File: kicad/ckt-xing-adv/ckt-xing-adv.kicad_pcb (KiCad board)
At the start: 2 copper layers, 76.2 x 63.5 mm, 49 parts, among them J1 Screw_Terminal_01x02, J2 SM04B-SRSS, J3 Conn_02x05_Counter_Clockwise, J4 SM04B-SRSS, J5 SM04B-SRSS, J6 Screw_Terminal_01x02, J7 Screw_Terminal_01x02, Q1 ZXMS6004FF, Q2 ZXMS6004FF, SW1 SW_DIP_x05, U1 PAM8301, U2 ATtiny861A-S, U3 AP7381-33Y, U4 W25Q128JVS

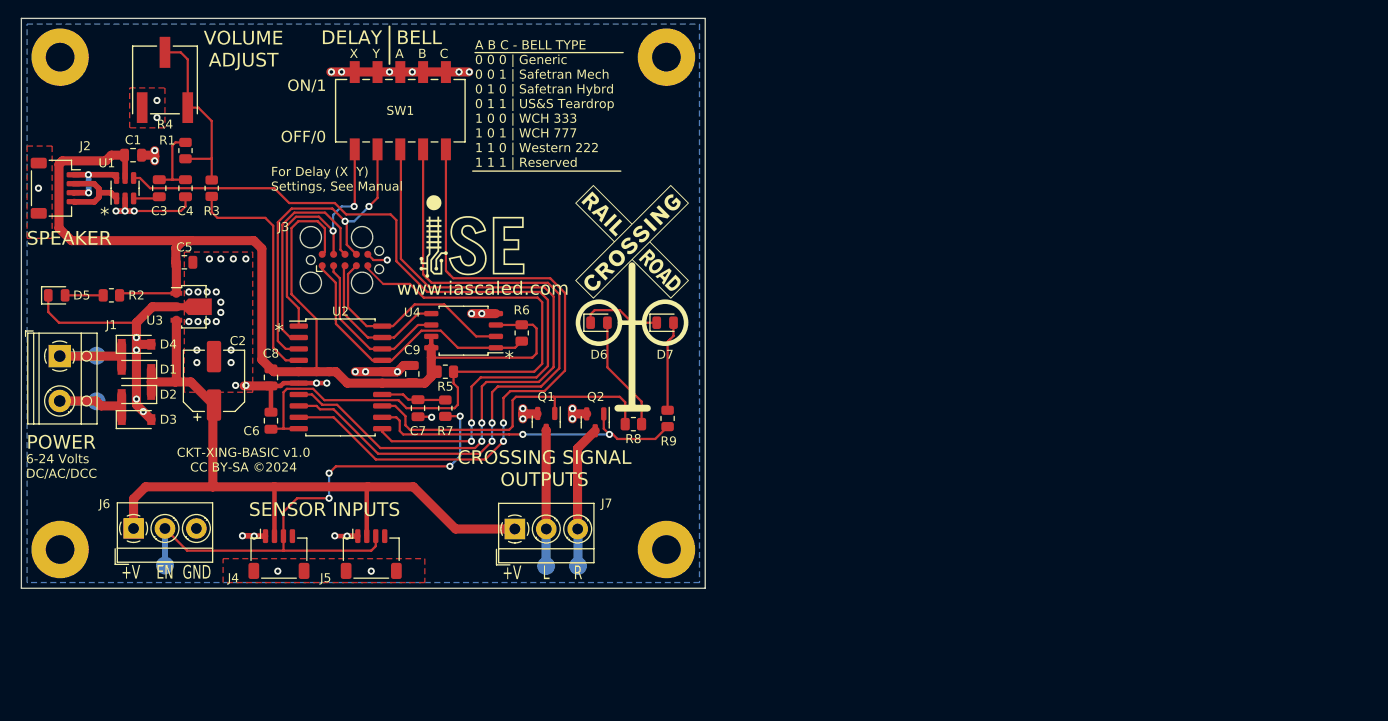
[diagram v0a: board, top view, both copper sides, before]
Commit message: Update advanced crossing with some fixes before PCB layout
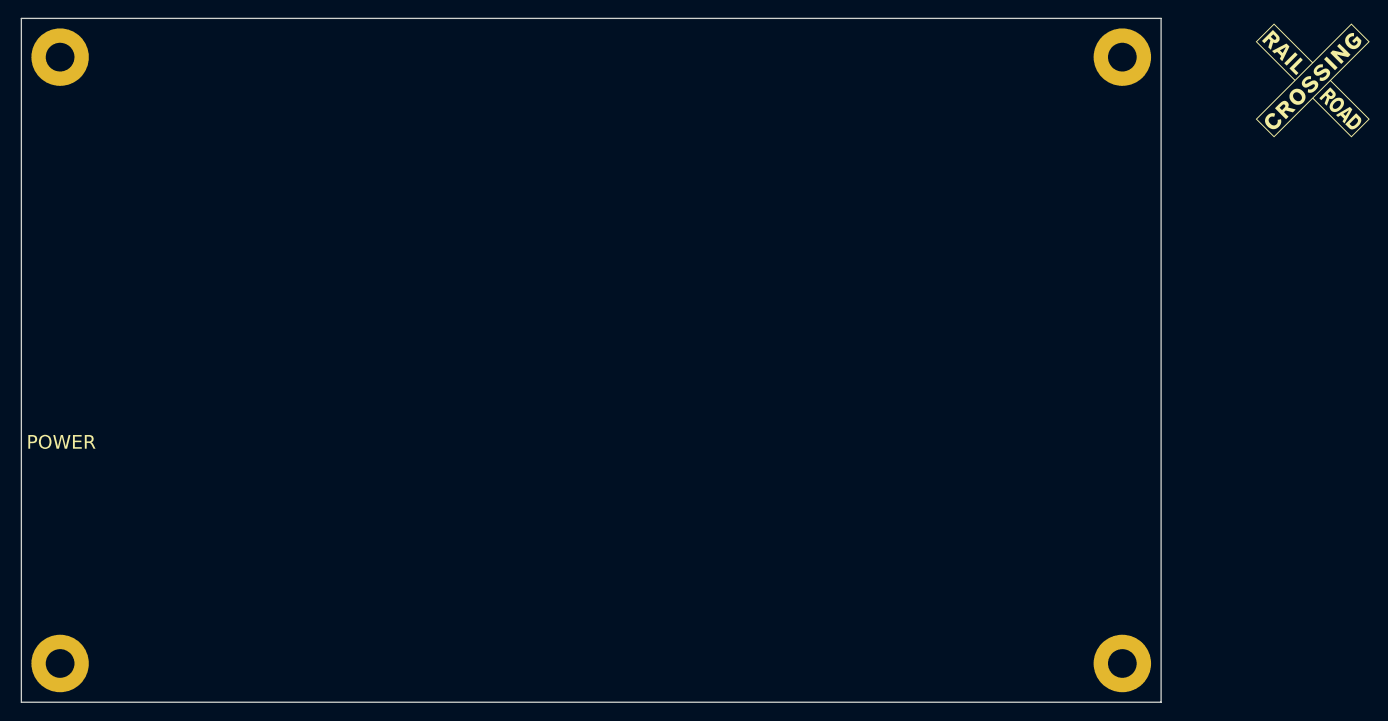
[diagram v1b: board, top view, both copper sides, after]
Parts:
- removed C1: 10uF, Capacitor_SMD:C_0805_2012Metric
- removed C2: 68uF, Capacitor_SMD:CP_Elec_6.3x5.8
- removed C3, C8, C9: 0.1uF, Capacitor_SMD:C_0805_2012Metric
- removed C4: 470pF, Capacitor_SMD:C_0805_2012Metric
- removed C5: 22uF, Capacitor_SMD:C_0805_2012Metric
- removed C6, C7: 1uF, Capacitor_SMD:C_0805_2012Metric
- removed D1, D2, D3, D4: CDBM140G, Diode_SMD:D_SOD-123
- removed D5: GREEN LED, LED_SMD:LED_0805_2012Metric
- removed D6, D7: RED LED, LED_SMD:LED_0805_2012Metric
- removed J1: Screw_Terminal_01x02, TerminalBlock_RND:TerminalBlock_RND_205-00012_1x02_P5.00mm_Horizontal
- removed J2, J4, J5: SM04B-SRSS, Connector_JST:JST_SH_SM04B-SRSS-TB_1x04-1MP_P1.00mm_Horizontal
- removed J3: Conn_02x05_Counter_Clockwise, Connector:Tag-Connect_TC2050-IDC-FP_2x05_P1.27mm_Vertical
- removed J6, J7: Screw_Terminal_01x02, TerminalBlock_MetzConnect:TerminalBlock_MetzConnect_Type059_RT06303HBWC_1x03_P3.50mm_Horizontal
- removed Q1, Q2: ZXMS6004FF, Package_TO_SOT_SMD:SOT-23
- removed R1: 100k, Resistor_SMD:R_0805_2012Metric
- removed R2, R7, R8, R9: 1k, Resistor_SMD:R_0805_2012Metric
- removed R3, R5, R6: 10k, Resistor_SMD:R_0805_2012Metric
- removed R4: 10k, ISE_UltraLibrarian:POT_3361P_BRN
- removed SW1: SW_DIP_x05, ISE_UltraLibrarian:CST_219SMT
- removed TP1, TP2, TP3, TP4, TP5: TestPoint, TestPoint:TestPoint_Pad_D2.0mm
- removed U1: PAM8301, Package_TO_SOT_SMD:SOT-23-6
- removed U2: ATtiny861A-S, Package_SO:SOIC-20W_7.5x12.8mm_P1.27mm
- removed U3: AP7381-33Y, ISE_Generic:SOT-89-3
- removed U4: W25Q128JVS, Package_SO:SOIC-8_5.23x5.23mm_P1.27mm
- moved G*** 77.9 mm to (169.3, 26.0)
- moved H2 52.4 mm to (148.1, 90.9)
- moved H3 50.8 mm to (148.1, 23.4)
- moved H4 12.7 mm to (29.7, 90.9)
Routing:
- net +3.3V: track 136.0 -> 0.00 mm
- net GND: track 106.0 -> 0.00 mm, vias 58 -> 0
- net /~{SD}: track 88.1 -> 0.00 mm, vias 2 -> 0
- net /VIN: track 84.9 -> 0.00 mm
- net /SW4: track 77.1 -> 0.00 mm, vias 2 -> 0
- net /SW3: track 77.0 -> 0.00 mm, vias 2 -> 0
- net /SW5: track 75.6 -> 0.00 mm, vias 2 -> 0
- net /~{RESET}: track 70.1 -> 0.00 mm
- net /EN1: track 63.7 -> 0.00 mm, vias 4 -> 0
- net /AVR_SCK: track 38.9 -> 0.00 mm, vias 2 -> 0
- net /OUT_L: track 36.6 -> 0.00 mm
- net /OUT_R: track 36.6 -> 0.00 mm, vias 2 -> 0
- net /~{FLASH_CS}: track 32.0 -> 0.00 mm
- net /AVR_MOSI: track 31.5 -> 0.00 mm, vias 2 -> 0
- net /PWM: track 26.3 -> 0.00 mm
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- removed copper zone on B.Cu, net GND
- removed copper zone on F.Cu, net GND
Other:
- board size 76.2 x 63.5 mm -> 127 x 76.2 mm
- board text removed: "*"
- board text removed: "+V"
- board text removed: "6-24 Volts DC/AC/DCC"
- board text removed: "A"
- board text removed: "A B C - BELL TYPE 0 0 0 | Generic 0 0 1 | Safetran Mech 0 1 0 | Safetran Hybrd 0 1 1 | US&S Teardrop 1 0 0 | WCH 333 1 0 1 | WCH 777 1 1 0 | Western 222 1 1 1 | Reserved"
- board text removed: "B"
- board text removed: "BELL"
- board text removed: "C"
- board text removed: "CKT-XING-BASIC v1.0 CC BY-SA ©2024"
- board text removed: "CROSSING SIGNAL OUTPUTS"
- board text removed: "DELAY"
- board text removed: "For Delay (X Y) Settings, See Manual"
- board text removed: "GND"
- board text removed: "L"
- board text removed: "R"
- board text removed: "SENSOR INPUTS"
- board text removed: "SPEAKER"
- board text removed: "VOLUME ADJUST"
- board text removed: "X"
- board text removed: "Y"
- board text removed: "www.iascaled.com"
- board text removed: "~{EN}"

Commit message: All nets routed on the ckt-xing-adv/ckt-xing-adv Still some DRC problems related to kicad 9
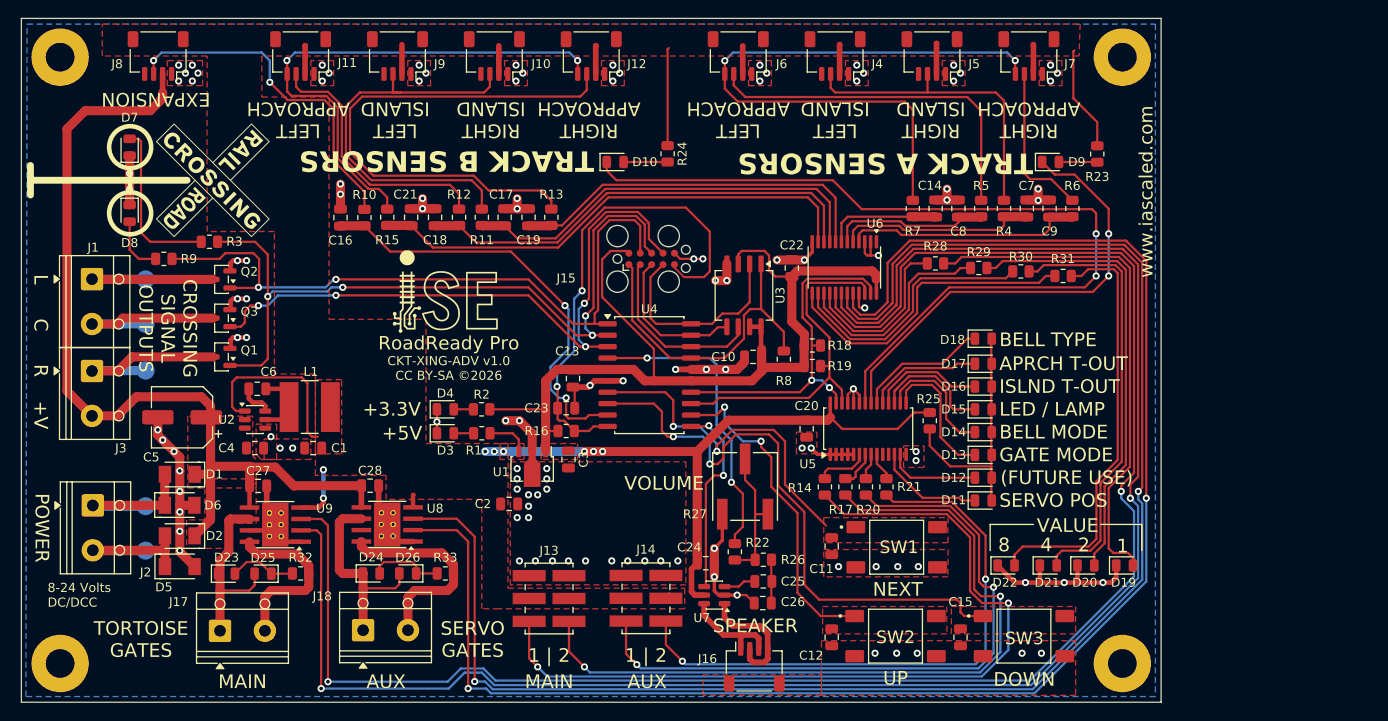
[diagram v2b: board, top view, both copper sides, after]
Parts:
- added C1: 22uF, Capacitor_SMD:C_0805_2012Metric, F.Cu at (57.9, 66.9)
- added C10: 0.1uF, Capacitor_SMD:C_0805_2012Metric, F.Cu at (106.9, 56.8)
- added C11: 0.1uF, Capacitor_SMD:C_0805_2012Metric, F.Cu at (115.7, 77.9)
- added C12: 0.1uF, Capacitor_SMD:C_0805_2012Metric, F.Cu at (115.7, 88.0)
- added C13: 0.1uF, Capacitor_SMD:C_0805_2012Metric, F.Cu at (86.9, 59.2)
- added C14: 1uF, Capacitor_SMD:C_0805_2012Metric, F.Cu at (127.3, 40.2)
- added C15: 0.1uF, Capacitor_SMD:C_0805_2012Metric, F.Cu at (130.0, 88.0)
- added C16: 1uF, Capacitor_SMD:C_0805_2012Metric, F.Cu at (61.0, 41.2)
- added C17: 1uF, Capacitor_SMD:C_0805_2012Metric, F.Cu at (79.2, 41.2)
- added C18: 1uF, Capacitor_SMD:C_0805_2012Metric, F.Cu at (71.5, 41.2)
- added C19: 1uF, Capacitor_SMD:C_0805_2012Metric, F.Cu at (81.9, 41.2)
- added C2: 22uF, Capacitor_SMD:C_0805_2012Metric, F.Cu at (79.8, 73.2)
- added C20: 1uF, Capacitor_SMD:C_0805_2012Metric, F.Cu at (112.9, 64.8)
- added C21: 1uF, Capacitor_SMD:C_0805_2012Metric, F.Cu at (68.8, 41.2)
- added C22: 0.1uF, Capacitor_SMD:C_0805_2012Metric, F.Cu at (111.3, 46.9)
- added C23: 1uF, Capacitor_SMD:C_0805_2012Metric, F.Cu at (86.1, 62.5)
- added C24: 10uF, Capacitor_SMD:C_0805_2012Metric, F.Cu at (101.7, 79.8)
- added C25: 0.1uF, Capacitor_SMD:C_0805_2012Metric, F.Cu at (108.1, 81.8)
- added C26: 470pF, Capacitor_SMD:C_0805_2012Metric, F.Cu at (108.0, 84.2)
- added C27: 1uF, Capacitor_SMD:C_0805_2012Metric, F.Cu at (51.8, 71.1)
- added C28: 1uF, Capacitor_SMD:C_0805_2012Metric, F.Cu at (64.3, 71.1)
- added C3: 22uF, Capacitor_SMD:C_0805_2012Metric, F.Cu at (86.4, 68.2)
- added C4: 10uF, Capacitor_SMD:C_0805_2012Metric, F.Cu at (51.4, 66.9)
- added C5: 68uF, Capacitor_SMD:CP_Elec_6.3x5.8, F.Cu at (43.3, 63.5)
- added C6: 0.1uF, Capacitor_SMD:C_0805_2012Metric, F.Cu at (51.7, 60.3)
- added C7: 1uF, Capacitor_SMD:C_0805_2012Metric, F.Cu at (137.4, 40.2)
- added C8: 1uF, Capacitor_SMD:C_0805_2012Metric, F.Cu at (129.8, 40.2)
- added C9: 1uF, Capacitor_SMD:C_0805_2012Metric, F.Cu at (140.0, 40.2)
- added D1: CDBM140G, ISE_Generic:SOD-123T, F.Cu at (43.1, 69.8)
- added D10: YELLOW, LED_SMD:LED_0805_2012Metric, F.Cu at (91.6, 35.1)
- added D11: YELLOW, LED_SMD:LED_0805_2012Metric, F.Cu at (132.6, 72.8)
- added D12: YELLOW, LED_SMD:LED_0805_2012Metric, F.Cu at (132.6, 70.2)
- added D13: YELLOW, LED_SMD:LED_0805_2012Metric, F.Cu at (132.6, 67.7)
- added D14: YELLOW, LED_SMD:LED_0805_2012Metric, F.Cu at (132.6, 65.2)
- added D15: BLUE, LED_SMD:LED_0805_2012Metric, F.Cu at (132.6, 62.6)
- added D16: YELLOW, LED_SMD:LED_0805_2012Metric, F.Cu at (132.6, 60.1)
- added D17: YELLOW, LED_SMD:LED_0805_2012Metric, F.Cu at (132.6, 57.5)
- added D18: YELLOW, LED_SMD:LED_0805_2012Metric, F.Cu at (132.6, 54.7)
- added D19: YELLOW, LED_SMD:LED_0805_2012Metric, F.Cu at (148.3, 80.0)
- added D2: CDBM140G, ISE_Generic:SOD-123T, F.Cu at (43.1, 76.7)
- added D20: YELLOW, LED_SMD:LED_0805_2012Metric, F.Cu at (144.0, 80.0)
- added D21: YELLOW, LED_SMD:LED_0805_2012Metric, F.Cu at (139.8, 80.0)
- added D22: YELLOW, LED_SMD:LED_0805_2012Metric, F.Cu at (135.1, 80.0)
- added D23: AMBER, LED_SMD:LED_0805_2012Metric, F.Cu at (48.3, 80.9)
- added D24: AMBER, LED_SMD:LED_0805_2012Metric, F.Cu at (64.4, 80.9)
- added D25: BLUE, LED_SMD:LED_0805_2012Metric, F.Cu at (52.3, 80.9)
- added D26: BLUE, LED_SMD:LED_0805_2012Metric, F.Cu at (68.5, 80.9)
- added D3: GREEN, LED_SMD:LED_0805_2012Metric, F.Cu at (72.6, 65.3)
- added D4: GREEN, LED_SMD:LED_0805_2012Metric, F.Cu at (72.6, 62.6)
- added D5: CDBM140G, ISE_Generic:SOD-123T, F.Cu at (43.1, 80.1)
- added D6: CDBM140G, ISE_Generic:SOD-123T, F.Cu at (43.0, 73.3)
- added D7: RED LED, LED_SMD:LED_0805_2012Metric, F.Cu at (37.5, 33.4)
- added D8: RED LED, LED_SMD:LED_0805_2012Metric, F.Cu at (37.5, 40.8)
- added D9: YELLOW, LED_SMD:LED_0805_2012Metric, F.Cu at (140.1, 35.1)
- added J1: Screw_Terminal_01x02, TerminalBlock_RND:TerminalBlock_RND_205-00012_1x02_P5.00mm_Horizontal, F.Cu at (33.3, 48.1)
- added J10: SM04B-SRSS, Connector_JST:JST_SH_SM04B-SRSS-TB_1x04-1MP_P1.00mm_Horizontal, F.Cu at (78.1, 23.2)
- added J11: SM04B-SRSS, Connector_JST:JST_SH_SM04B-SRSS-TB_1x04-1MP_P1.00mm_Horizontal, F.Cu at (56.5, 23.2)
- added J12: SM04B-SRSS, Connector_JST:JST_SH_SM04B-SRSS-TB_1x04-1MP_P1.00mm_Horizontal, F.Cu at (88.9, 23.2)
- added J13: Conn_02x03_Row_Letter_First, ISE_UltraLibrarian:MOLEX_15910060, F.Cu at (84.2, 83.7)
- added J14: Conn_02x03_Row_Letter_First, ISE_UltraLibrarian:MOLEX_15910060, F.Cu at (95.0, 83.7)
- added J15: Conn_02x05_Counter_Clockwise, Connector:Tag-Connect_TC2050-IDC-FP_2x05_P1.27mm_Vertical, F.Cu at (95.6, 45.8)
- added J16: SM04B-SRSS, Connector_JST:JST_SH_SM04B-SRSS-TB_1x04-1MP_P1.00mm_Horizontal, F.Cu at (107.1, 91.3)
- added J17: Screw_Terminal_01x02, TerminalBlock_RND:TerminalBlock_RND_205-00012_1x02_P5.00mm_Horizontal, F.Cu at (47.5, 87.3)
- added J18: Screw_Terminal_01x02, TerminalBlock_RND:TerminalBlock_RND_205-00012_1x02_P5.00mm_Horizontal, F.Cu at (63.5, 87.2)
- added J2: Screw_Terminal_01x02, TerminalBlock_RND:TerminalBlock_RND_205-00012_1x02_P5.00mm_Horizontal, F.Cu at (33.4, 73.3)
- added J3: Screw_Terminal_01x02, TerminalBlock_RND:TerminalBlock_RND_205-00012_1x02_P5.00mm_Horizontal, F.Cu at (33.3, 58.3)
- added J4: SM04B-SRSS, Connector_JST:JST_SH_SM04B-SRSS-TB_1x04-1MP_P1.00mm_Horizontal, F.Cu at (116.1, 23.2)
- added J5: SM04B-SRSS, Connector_JST:JST_SH_SM04B-SRSS-TB_1x04-1MP_P1.00mm_Horizontal, F.Cu at (126.9, 23.2)
- added J6: SM04B-SRSS, Connector_JST:JST_SH_SM04B-SRSS-TB_1x04-1MP_P1.00mm_Horizontal, F.Cu at (105.3, 23.2)
- added J7: SM04B-SRSS, Connector_JST:JST_SH_SM04B-SRSS-TB_1x04-1MP_P1.00mm_Horizontal, F.Cu at (137.7, 23.2)
- added J8: SM04B-SRSS, Connector_JST:JST_SH_SM04B-SRSS-TB_1x04-1MP_P1.00mm_Horizontal, F.Cu at (40.6, 23.2)
- added J9: SM04B-SRSS, Connector_JST:JST_SH_SM04B-SRSS-TB_1x04-1MP_P1.00mm_Horizontal, F.Cu at (67.3, 23.2)
- added L1: 4.7uH, ISE_UltraLibrarian:MSS6132-xxxMLC, F.Cu at (57.5, 62.4)
- added Q1: ZXMS6004FF, Package_TO_SOT_SMD:SOT-23, F.Cu at (47.7, 56.8)
- added Q2: ZXMS6004FF, Package_TO_SOT_SMD:SOT-23, F.Cu at (47.7, 48.1)
- added Q3: ZXMS6004FF, Package_TO_SOT_SMD:SOT-23, F.Cu at (47.7, 52.5)
- added R1: 1k, Resistor_SMD:R_0805_2012Metric, F.Cu at (76.7, 65.3)
- added R10: 1k, Resistor_SMD:R_0805_2012Metric, F.Cu at (63.6, 41.2)
- added R11: 1k, Resistor_SMD:R_0805_2012Metric, F.Cu at (76.7, 41.2)
- added R12: 1k, Resistor_SMD:R_0805_2012Metric, F.Cu at (74.2, 41.2)
- added R13: 1k, Resistor_SMD:R_0805_2012Metric, F.Cu at (84.5, 41.2)
- added R14: 1k, Resistor_SMD:R_0805_2012Metric, F.Cu at (114.9, 71.2)
- added R15: 1k, Resistor_SMD:R_0805_2012Metric, F.Cu at (66.2, 41.2)
- added R16: 10k, Resistor_SMD:R_0805_2012Metric, F.Cu at (86.1, 65.0)
- added R17: 1k, Resistor_SMD:R_0805_2012Metric, F.Cu at (117.2, 71.2)
- added R18: 10k, Resistor_SMD:R_0805_2012Metric, F.Cu at (113.5, 55.5)
- added R19: 10k, Resistor_SMD:R_0805_2012Metric, F.Cu at (113.5, 57.8)
- added R2: 1k, Resistor_SMD:R_0805_2012Metric, F.Cu at (76.7, 62.6)
- added R20: 1k, Resistor_SMD:R_0805_2012Metric, F.Cu at (119.5, 71.2)
- added R21: 1k, Resistor_SMD:R_0805_2012Metric, F.Cu at (121.8, 71.2)
- added R22: 10k, Resistor_SMD:R_0805_2012Metric, F.Cu at (104.9, 78.5)
- added R23: 1k, Resistor_SMD:R_0805_2012Metric, F.Cu at (145.3, 34.2)
- added R24: 1k, Resistor_SMD:R_0805_2012Metric, F.Cu at (97.4, 34.1)
- added R25: 1k, Resistor_SMD:R_0805_2012Metric, F.Cu at (126.6, 63.9)
- added R26: 100k, Resistor_SMD:R_0805_2012Metric, F.Cu at (108.1, 79.4)
- added R27: 10k, ISE_UltraLibrarian:POT_3361P_BRN, F.Cu at (106.0, 71.2)
- added R28: 1k, Resistor_SMD:R_0805_2012Metric, F.Cu at (127.3, 46.4)
- added R29: 1k, Resistor_SMD:R_0805_2012Metric, F.Cu at (132.1, 46.9)
- added R3: 1k, Resistor_SMD:R_0805_2012Metric, F.Cu at (46.4, 43.9)
- added R30: 1k, Resistor_SMD:R_0805_2012Metric, F.Cu at (136.8, 47.2)
- added R31: 1k, Resistor_SMD:R_0805_2012Metric, F.Cu at (141.5, 47.8)
- added R32: 1k, Resistor_SMD:R_0805_2012Metric, F.Cu at (56.5, 80.9)
- added R33: 1k, Resistor_SMD:R_0805_2012Metric, F.Cu at (72.6, 80.9)
- added R4: 1k, Resistor_SMD:R_0805_2012Metric, F.Cu at (134.9, 40.2)
- added R5: 1k, Resistor_SMD:R_0805_2012Metric, F.Cu at (132.4, 40.2)
- added R6: 1k, Resistor_SMD:R_0805_2012Metric, F.Cu at (142.5, 40.2)
- added R7: 1k, Resistor_SMD:R_0805_2012Metric, F.Cu at (124.7, 40.2)
- added R8: 10k, Resistor_SMD:R_0805_2012Metric, F.Cu at (110.4, 57.0)
- added R9: 1k, Resistor_SMD:R_0805_2012Metric, F.Cu at (41.3, 45.8)
- added SW1: FSM4JSMATR, ISE_Generic:TE_FSM4JSMA, F.Cu at (122.9, 78.0)
- added SW2: FSM4JSMATR, ISE_Generic:TE_FSM4JSMA, F.Cu at (122.8, 87.9)
- added SW3: FSM4JSMATR, ISE_Generic:TE_FSM4JSMA, F.Cu at (137.1, 87.9)
- added TP1: TestPoint, TestPoint:TestPoint_Pad_D2.0mm, B.Cu at (39.2, 58.3)
- added TP2: TestPoint, TestPoint:TestPoint_Pad_D2.0mm, B.Cu at (39.2, 73.4)
- added TP3: TestPoint, TestPoint:TestPoint_Pad_D2.0mm, B.Cu at (39.2, 78.4)
- added TP4: TestPoint, TestPoint:TestPoint_Pad_D2.0mm, B.Cu at (39.2, 48.1)
- added TP5: TestPoint, TestPoint:TestPoint_Pad_D2.0mm, B.Cu at (39.2, 53.1)
- added U1: AP7381-33Y, ISE_Generic:SOT-89-3, F.Cu at (82.3, 69.0)
- added U2: AP63205WU, Package_TO_SOT_SMD:TSOT-23-6, F.Cu at (51.4, 63.8)
- added U3: W25Q128JVS, Package_SO:SOIC-8_5.3x6.2mm_P1.27mm, F.Cu at (105.9, 49.9)
- added U4: ATtiny861A-S, Package_SO:SOIC-20W_7.5x12.8mm_P1.27mm, F.Cu at (95.4, 58.8)
- added U5: PCA9685PW, Package_SO:TSSOP-28_4.4x9.7mm_P0.65mm, F.Cu at (119.8, 64.8)
- added U6: PCA9555D, Package_SO:TSSOP-24_4.4x7.8mm_P0.65mm, F.Cu at (117.1, 46.8)
- added U7: PAM8301, Package_TO_SOT_SMD:SOT-23-6, F.Cu at (102.6, 83.3)
- added U8: DRV8231A, Package_SO:Texas_HTSOP-8-1EP_3.9x4.9mm_P1.27mm_EP2.95x4.9mm_Mask2.4x3.1mm_ThermalVias, F.Cu at (66.2, 75.4)
- added U9: DRV8231A, Package_SO:Texas_HTSOP-8-1EP_3.9x4.9mm_P1.27mm_EP2.95x4.9mm_Mask2.4x3.1mm_ThermalVias, F.Cu at (53.7, 75.5)
- moved G*** 123.1 mm to (46.7, 37.1), turned to -90 degrees
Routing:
- net /GATE_M2: track 0.00 -> 194.6 mm, vias 0 -> 2
- net /GATE_M1: track 0.00 -> 194.6 mm, vias 0 -> 2
- net /GATE_X2: track 0.00 -> 181.2 mm, vias 0 -> 2
- net /GATE_X1: track 0.00 -> 181.1 mm, vias 0 -> 2
- net GND: track 0.00 -> 160.5 mm, vias 0 -> 116
- net +5V: track 0.00 -> 154.7 mm, vias 0 -> 8
- net /VIN: track 0.00 -> 106.0 mm
- net +3.3V: track 0.00 -> 104.5 mm
- net Net-(D10-K): track 0.00 -> 98.1 mm, vias 0 -> 2
- net Net-(J13-Pin_a1): track 0.00 -> 93.8 mm, vias 0 -> 2
- net /AVR_MISO: track 0.00 -> 85.5 mm, vias 0 -> 4
- net Net-(J13-Pin_b1): track 0.00 -> 85.0 mm, vias 0 -> 2
- net /AVR_MOSI: track 0.00 -> 76.9 mm, vias 0 -> 2
- net Net-(J14-Pin_a1): track 0.00 -> 74.9 mm, vias 0 -> 2
- net /AVR_SCK: track 0.00 -> 72.5 mm, vias 0 -> 4
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- added copper zone on F.Cu, net +3.3V
- added copper zone on F.Cu, net +5V
- added copper zone on F.Cu, net /SW_DOWN
- added copper zone on F.Cu, net /SW_NEXT
- added copper zone on F.Cu, net /SW_UP
- added copper zone on F.Cu, net /VIN
- added copper zone on B.Cu, net GND
- added copper zone on F.Cu, net GND
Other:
- board text added: "(FUTURE USE)"
- board text added: "+3.3V"
- board text added: "+5V"
- board text added: "+V"
- board text added: "1"
- board text added: "1 | 2"
- board text added: "2"
- board text added: "4"
- board text added: "8"
- board text added: "8-24 Volts DC/DCC"
- board text added: "APRCH T-OUT"
- board text added: "AUX"
- board text added: "BELL MODE"
- board text added: "BELL TYPE"
- board text added: "C"
- board text added: "CKT-XING-ADV v1.0 CC BY-SA ©2026"
- board text added: "CROSSING SIGNAL OUTPUTS"
- board text added: "DOWN"
- board text added: "EXPANSION"
- board text added: "GATE MODE"
- board text added: "ISLND T-OUT"
- board text added: "L"
- board text added: "LED / LAMP"
- board text added: "LEFT APPROACH"
- board text added: "LEFT ISLAND"
- board text added: "MAIN"
- board text added: "NEXT"
- board text added: "R"
- board text added: "RIGHT APPROACH"
- board text added: "RIGHT ISLAND"
- board text added: "RoadReady Pro"
- board text added: "SERVO GATES"
- board text added: "SERVO POS"
- board text added: "SPEAKER"
- board text added: "TORTOISE GATES"
- board text added: "TRACK A SENSORS"
- board text added: "TRACK B SENSORS"
- board text added: "UP"
- board text added: "VALUE"
- board text added: "VOLUME"
- board text added: "www.iascaled.com"
